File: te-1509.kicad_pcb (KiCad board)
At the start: 2 copper layers, 46.6 x 29.2 mm, 12 parts, among them CN1 ce-connector, SW1 SP3T, U1 AS6C1008, U2 CD4572

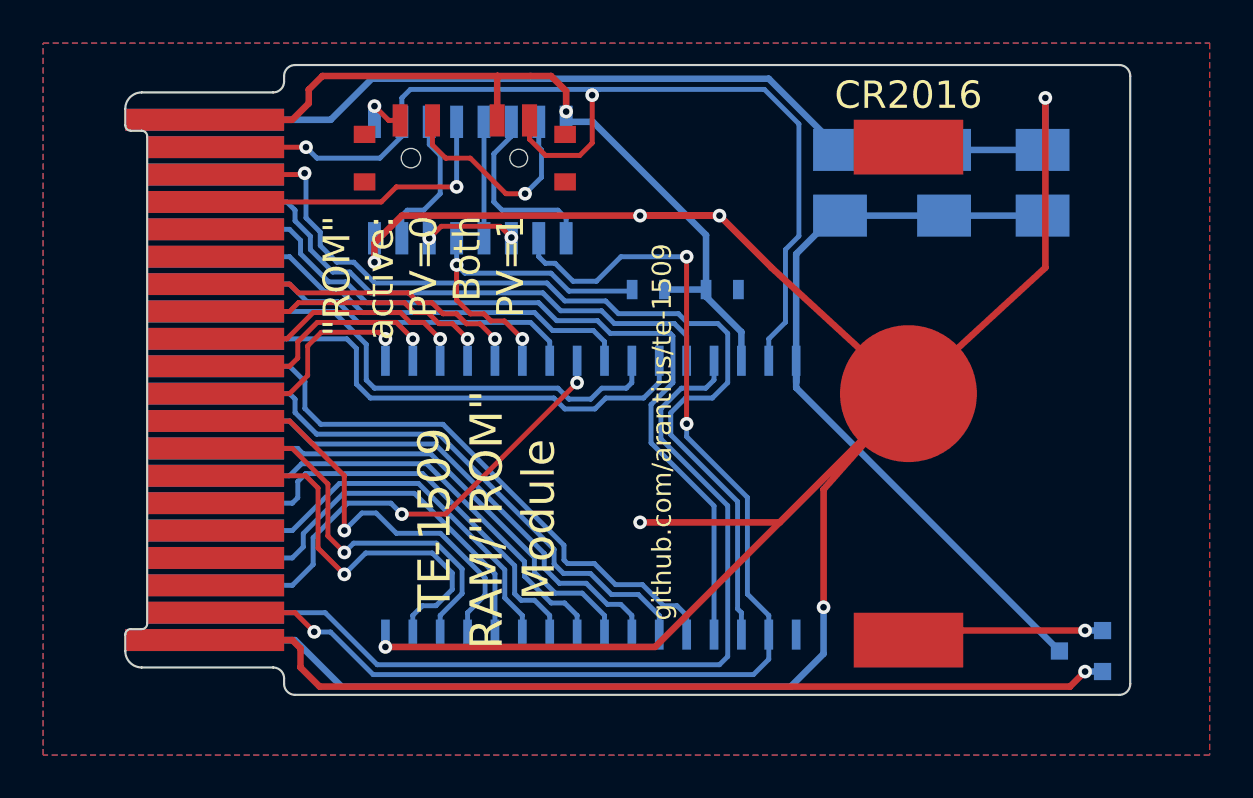
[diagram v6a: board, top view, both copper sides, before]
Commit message: tweak footprints based on physical components
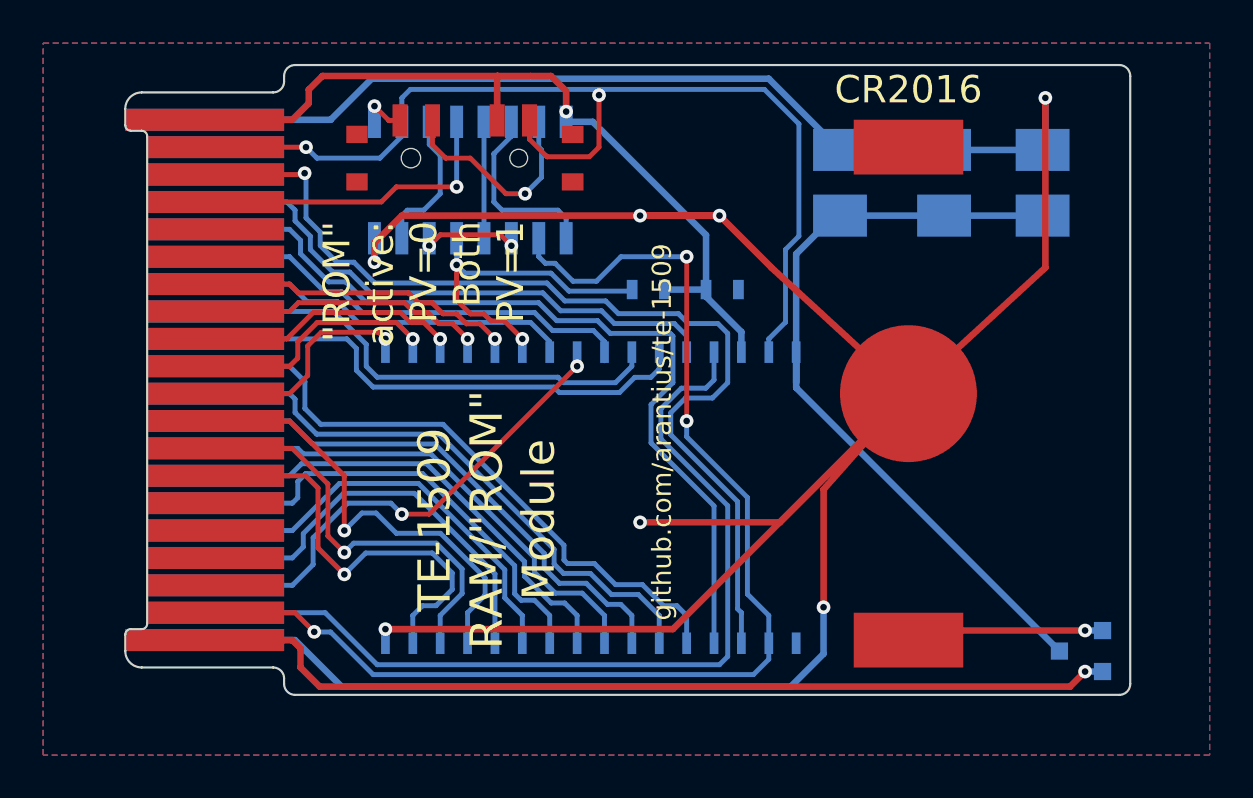
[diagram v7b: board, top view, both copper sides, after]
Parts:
- SW1: footprint te-1509:EG1300 -> EG1300
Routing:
- net /AD9: track 23.3 -> 22.2 mm
- net /AD8: track 24.4 -> 23.4 mm
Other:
- rule trace_min: 0.2286 -> 0.009
- rule via_min_size: 0.635 -> 0.025
